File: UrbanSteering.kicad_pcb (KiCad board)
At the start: 2 copper layers, 144 x 100 mm, 47 parts, among them J1 Joystick, J2 Main_conn, J3 CAN_term, J4 STM32L432, J5 Screen_Left, J6 Screen_Right, J9 Proximity_sensor, U1 MCP2562, U2 74HC595PW, U3 74HC597D

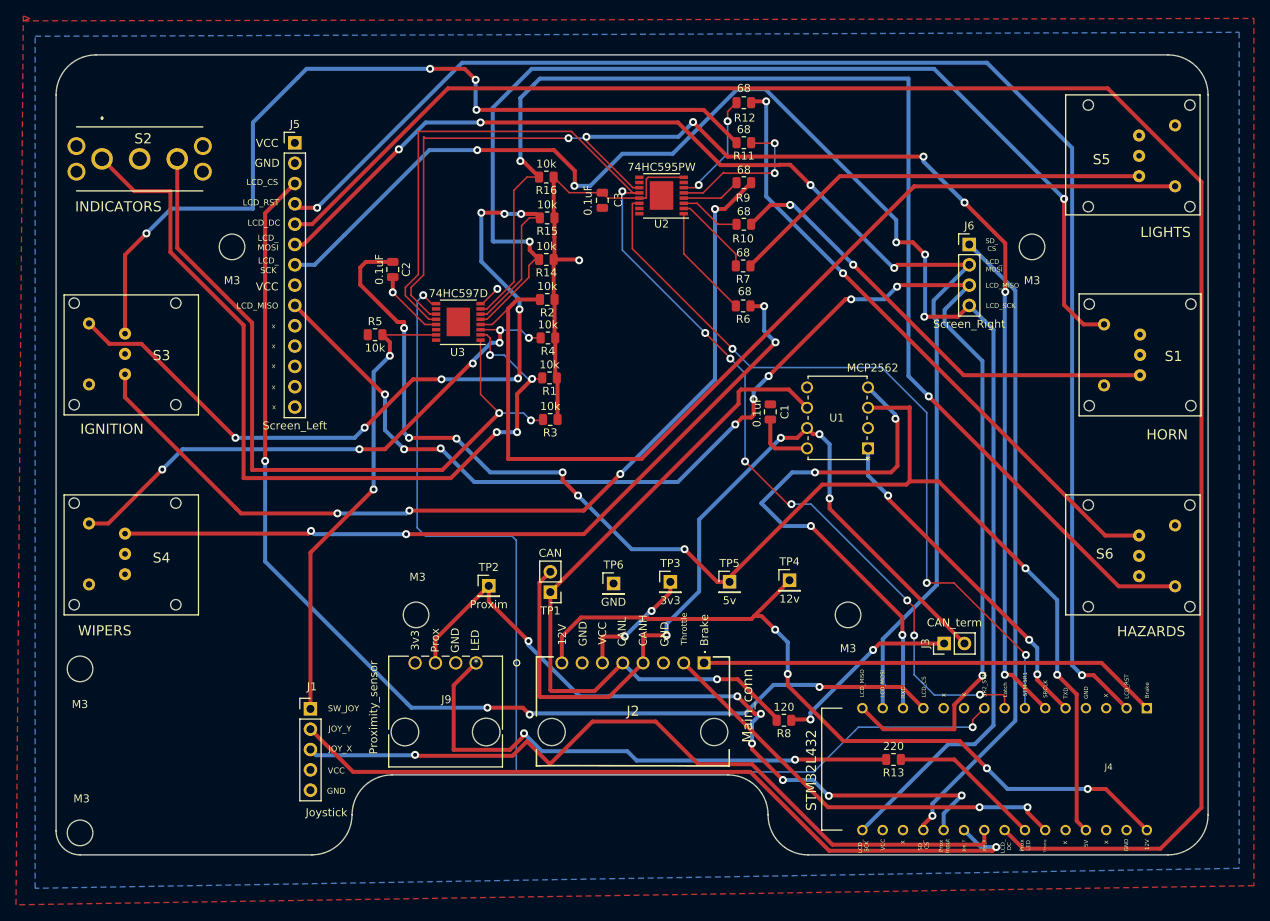
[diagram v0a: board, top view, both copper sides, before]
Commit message: updated clearance settings and connected some non-contiguous filled zones
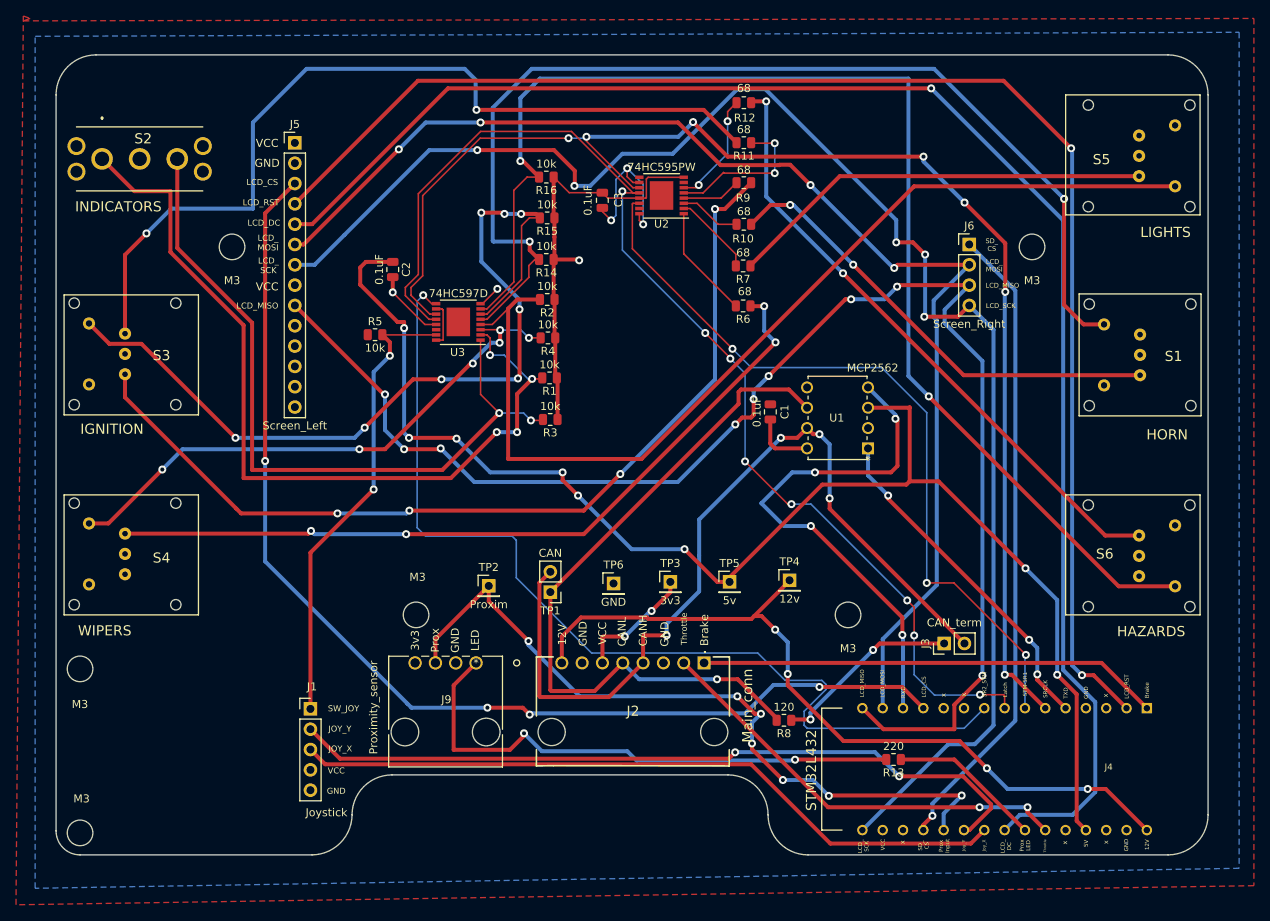
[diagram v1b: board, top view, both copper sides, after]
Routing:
- net /LCD_DC: track 231.1 -> 196.3 mm, vias 0 -> 1
- net VCC: track 15.3 -> 42.4 mm, vias 2 -> 5
- net /SR2-STM: track 135.8 -> 123.3 mm, vias 2 -> 1
- net /JoystickX: track 96.8 -> 89.8 mm, vias 1 -> 0
- net /Latch: track 150.6 -> 146.0 mm
- net /SRCLK: track 175.2 -> 170.8 mm
- net /JoystickY: track 97.1 -> 94.7 mm, vias 1 -> 2
- net /LCD_RST: track 183.0 -> 180.7 mm
- net Net-(R11-Pad2): vias 4 -> 2

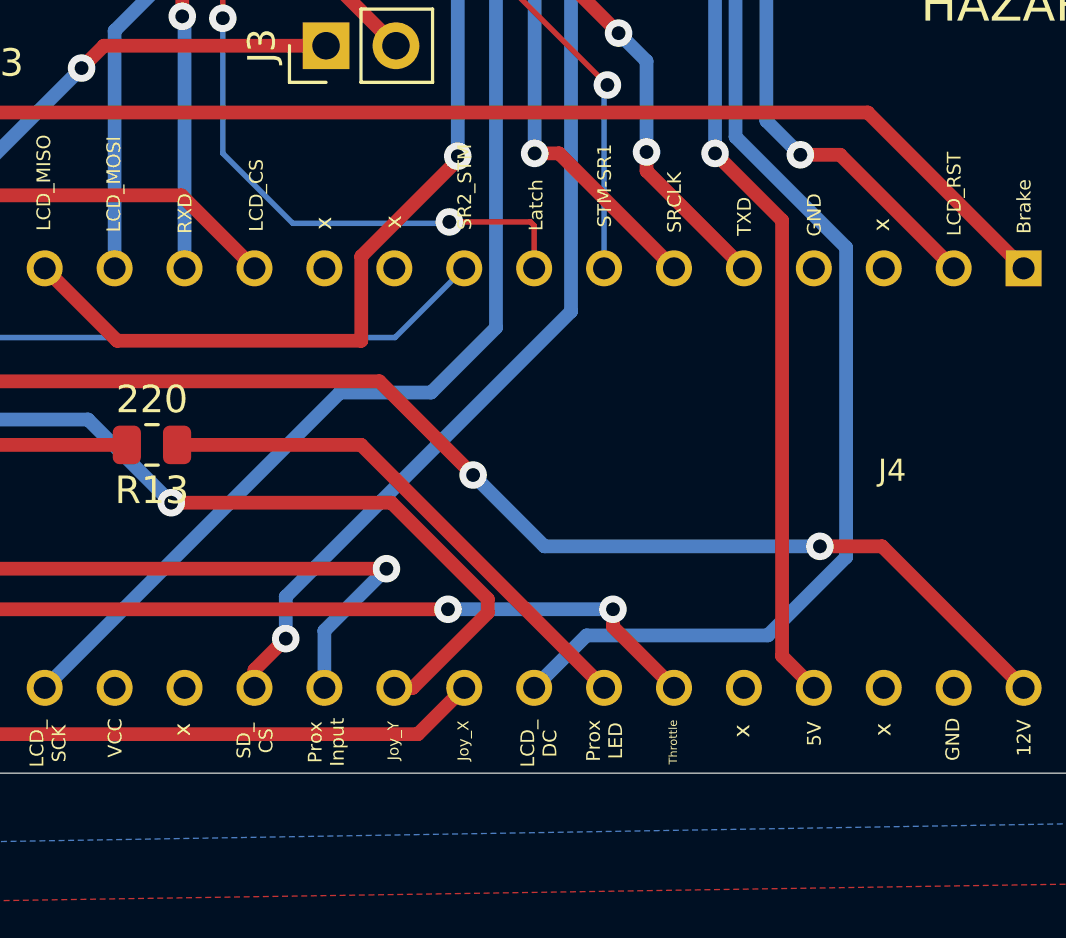
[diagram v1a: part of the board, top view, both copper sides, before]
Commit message: added label names on STM
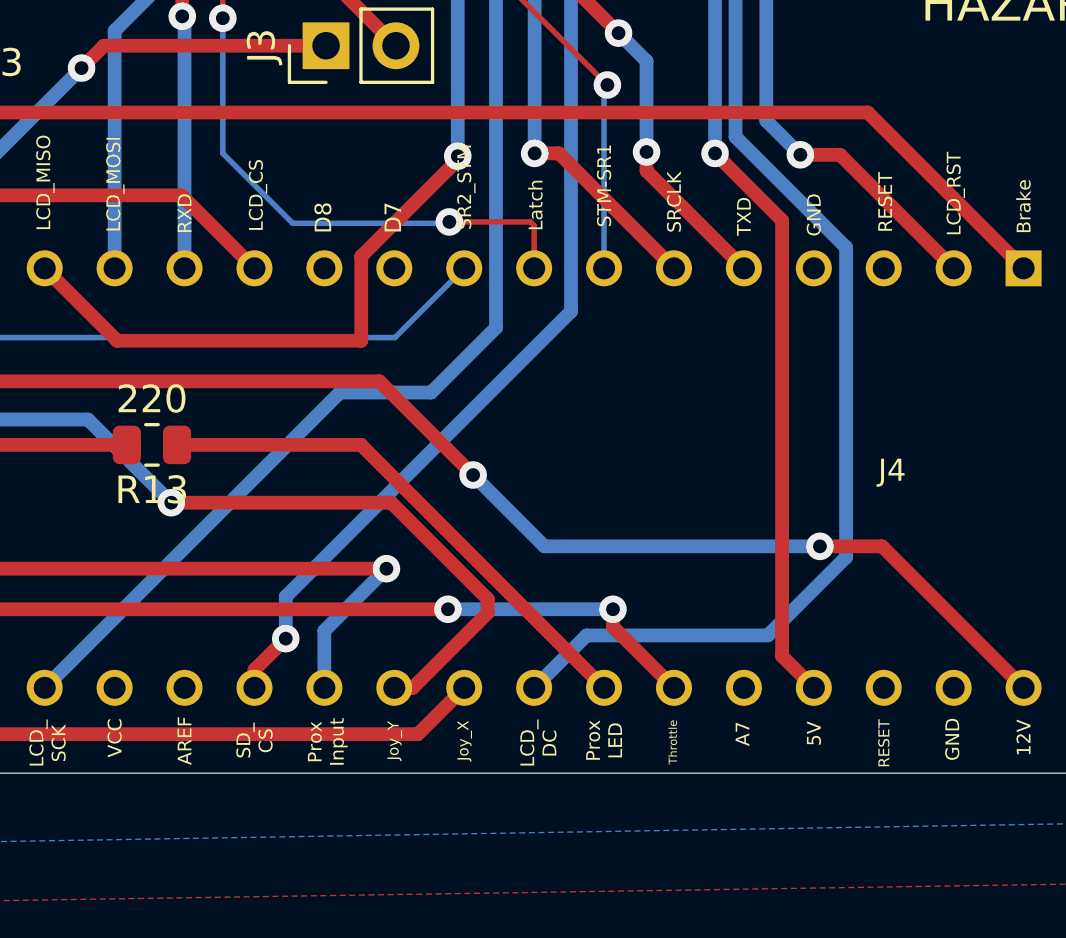
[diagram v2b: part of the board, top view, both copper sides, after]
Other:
- board text added: "A7"
- board text added: "AREF"
- board text added: "D7"
- board text added: "D8"
- board text added: "RESET"
- board text removed: "x"
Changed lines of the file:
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@@
   (gr_arc (start 194 150) (mid 190.464466 148.535534) (end 189 145) (layer "Edge.Cuts") (width 0.05))
   (gr_line (start 105 50) (end 239 50) (layer "Edge.Cuts") (width 0.0015))
-  (gr_text "x" (at 213.457979 129.97434 90) (layer "F.SilkS")
+  (gr_text "D7" (at 213.457979 129.82194 90) (layer "F.SilkS")
     (effects (font (size 0.6 0.6) (thickness 0.1)))
   )
@@
     (effects (font (size 0.5 0.5) (thickness 0.1)))
   )
-  (gr_text "x" (at 231.237979 148.41474 90) (layer "F.SilkS")
-    (effects (font (size 0.6 0.6) (thickness 0.1)))
+  (gr_text "RESET" (at 231.288779 148.92274 90) (layer "F.SilkS")
+    (effects (font (size 0.4 0.4) (thickness 0.08)))
   )
   (gr_text "Latch" (at 218.639579 129.36474 90) (layer "F.SilkS")
@@
     (effects (font (size 0.5 0.5) (thickness 0.1)))
   )
-  (gr_text "x" (at 205.787179 148.41474 90) (layer "F.SilkS")
-    (effects (font (size 0.6 0.6) (thickness 0.1)))
+  (gr_text "AREF" (at 205.888779 148.82114 90) (layer "F.SilkS")
+    (effects (font (size 0.5 0.5) (thickness 0.1)))
   )
   (gr_text "Prox\nLED\n" (at 221.128779 148.82114 90) (layer "F.SilkS")
@@
     (effects (font (size 0.75 0.75) (thickness 0.15)))
   )
-  (gr_text "x" (at 231.187179 130.07594 90) (layer "F.SilkS")
-    (effects (font (size 0.6 0.6) (thickness 0.1)))
+  (gr_text "RESET" (at 231.339579 129.26314 90) (layer "F.SilkS")
+    (effects (font (size 0.5 0.5) (thickness 0.1)))
   )
   (gr_text "GND" (at 165.858379 122.35434 90) (layer "F.SilkS")
@@
     (effects (font (size 0.5 0.5) (thickness 0.1)))
   )
-  (gr_text "x" (at 226.107179 148.46554 90) (layer "F.SilkS")
-    (effects (font (size 0.6 0.6) (thickness 0.1)))
+  (gr_text "A7" (at 226.157979 148.56714 90) (layer "F.SilkS")
+    (effects (font (size 0.5 0.5) (thickness 0.1)))
   )
   (gr_text "JOY_X" (at 135.530779 136.73074) (layer "F.SilkS")
@@
     (effects (font (size 0.5 0.5) (thickness 0.1)))
   )
-  (gr_text "x" (at 210.917979 130.02514 90) (layer "F.SilkS")
+  (gr_text "D8" (at 210.917979 129.82194 90) (layer "F.SilkS")
     (effects (font (size 0.6 0.6) (thickness 0.1)))
   )

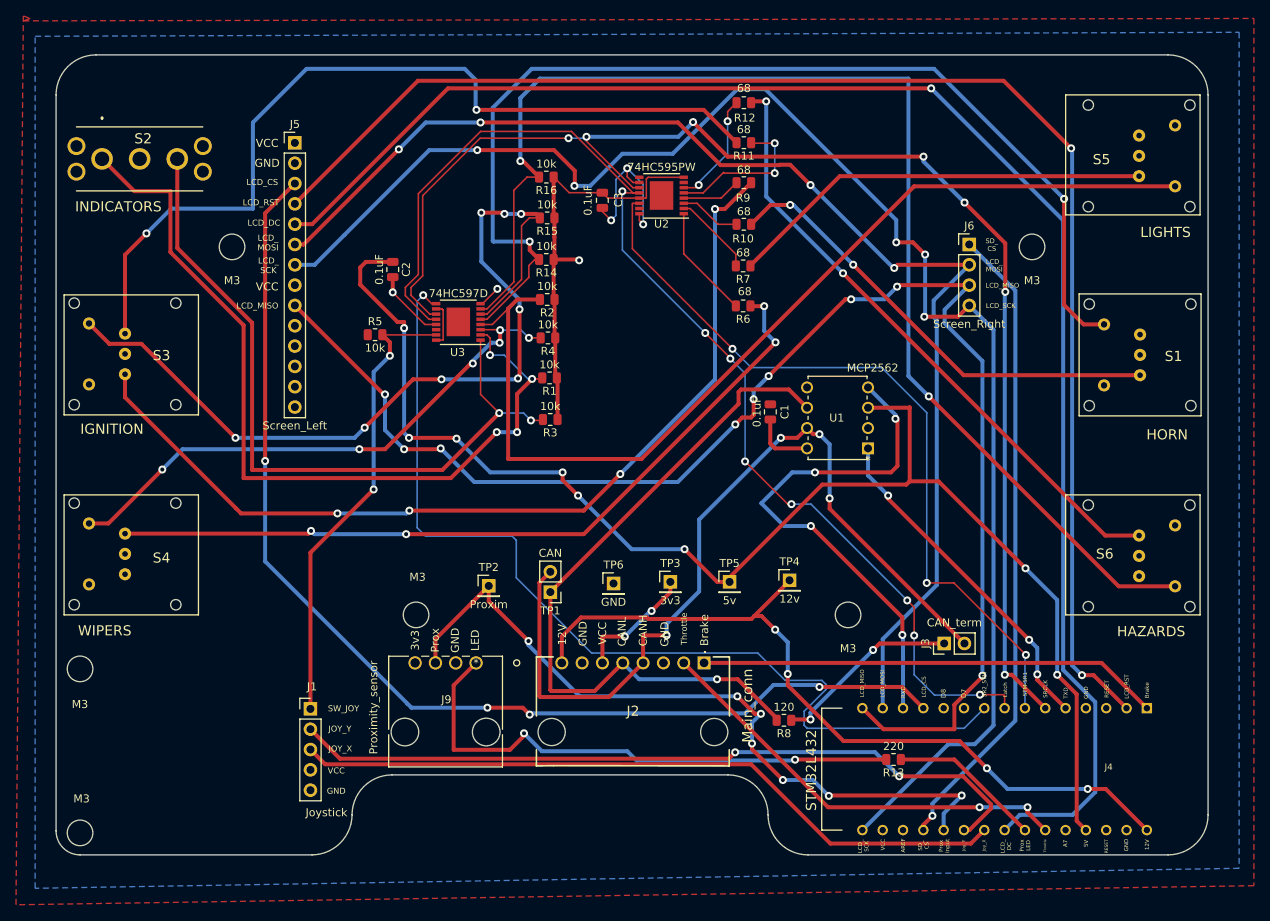
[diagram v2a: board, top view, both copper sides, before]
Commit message: added fuse to schematic - layout to be changed
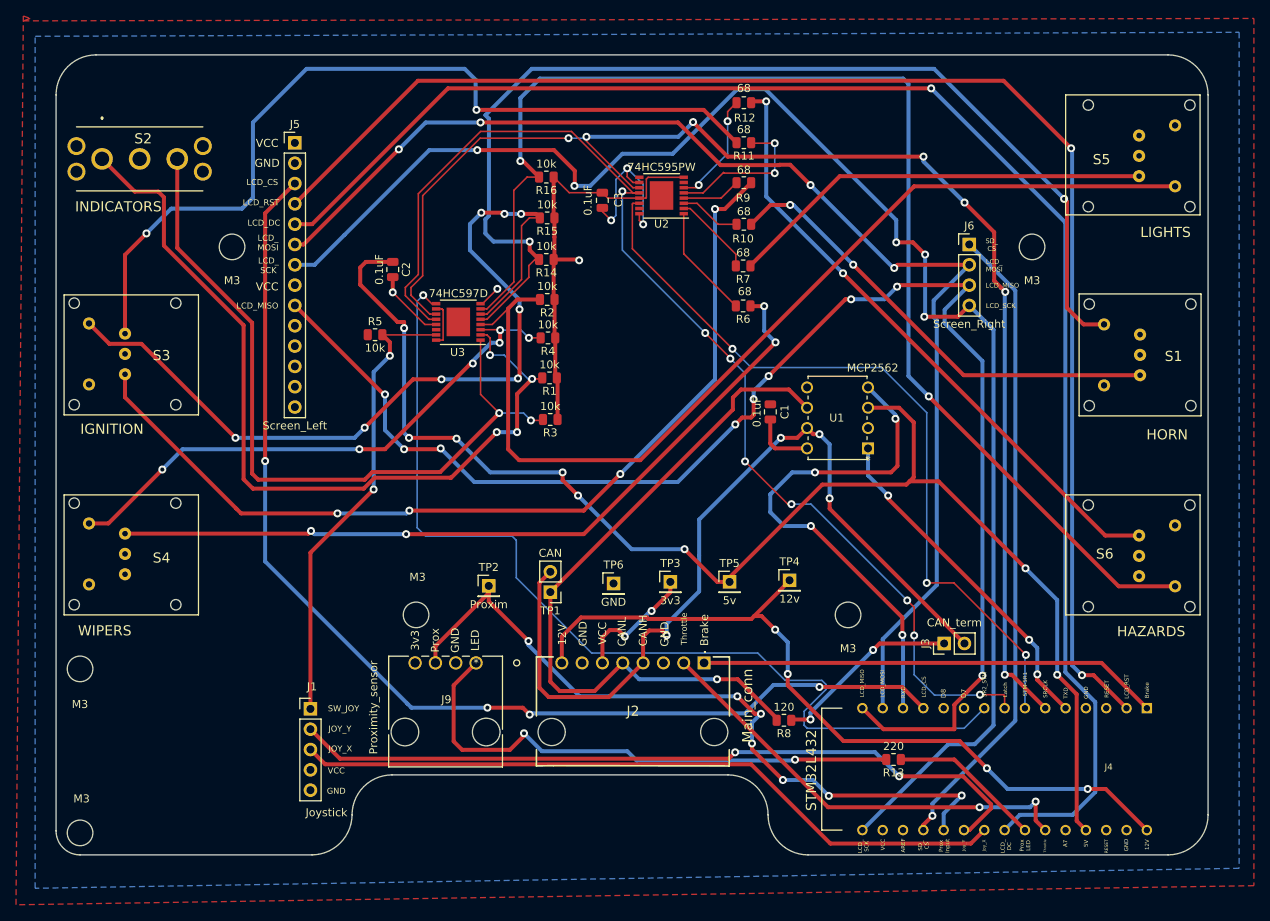
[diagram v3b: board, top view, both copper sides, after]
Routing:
- net /Throttle: track 54.2 -> 55.8 mm
- net /BTN_IND_RIGHT: track 92.6 -> 93.8 mm
- net /BTN_IGNITION: track 109.3 -> 110.5 mm
- net /BTN_HORN: track 134.7 -> 135.8 mm
- net /RXD: track 65.2 -> 64.3 mm
- net Net-(R11-Pad2): track 108.2 -> 107.4 mm
- net VCC: track 42.4 -> 43.1 mm
- net /CANL: track 89.6 -> 88.9 mm
- net Net-(J9-Pad1): track 68.6 -> 68.0 mm
- net /BTN_LIGHTS: track 125.0 -> 124.4 mm

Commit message: added labels
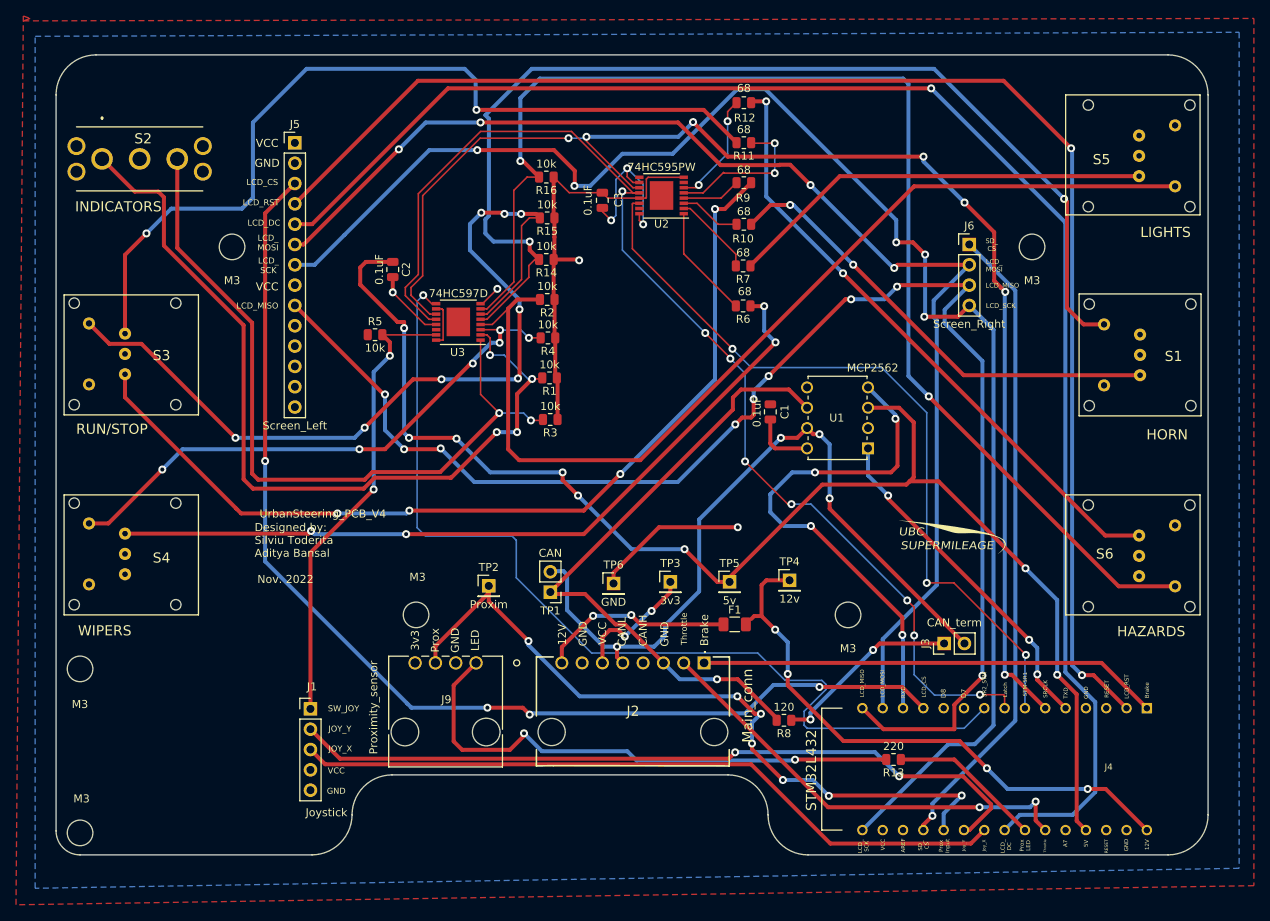
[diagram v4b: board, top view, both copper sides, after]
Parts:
- added F1: Fuse, Fuse:Fuse_1206_3216Metric, F.Cu at (184.8, 121.2)
- added SUPERMILEAGE: LOGO, Supermileage_PCB:Logo_bitmap, F.Cu at (211.7, 110.7)
- S3: value IGNITION -> RUN/STOP
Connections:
- J2 pad 3: GND -> /CANL
- J2 pad 4: /CANH -> GND
- J2 pad 5: /CANL -> /CANH
- J2 pad 8: +12V -> Net-(J2-Pad8)
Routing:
- net +12V: track 98.2 -> 71.4 mm
- net Net-(J2-Pad8): track 0.00 -> 24.3 mm, vias 0 -> 2
- net GND: track 73.3 -> 92.5 mm, vias 3 -> 4
- net /CANH: track 107.0 -> 93.8 mm
- net /CANL: track 88.9 -> 79.5 mm
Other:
- board text added: "Designed by: Silviu Toderita Aditya Bansal"
- board text added: "Nov. 2022"
- board text added: "UBC"
- board text added: "UrbanSteering_PCB_V4"
